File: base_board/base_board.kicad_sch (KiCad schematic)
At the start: 22 parts, among them J1 Conn_ARM_JTAG_SWD_20, U1 STM32F446ZEJx, U2 IS42S16400J-xT, U3 BMI270

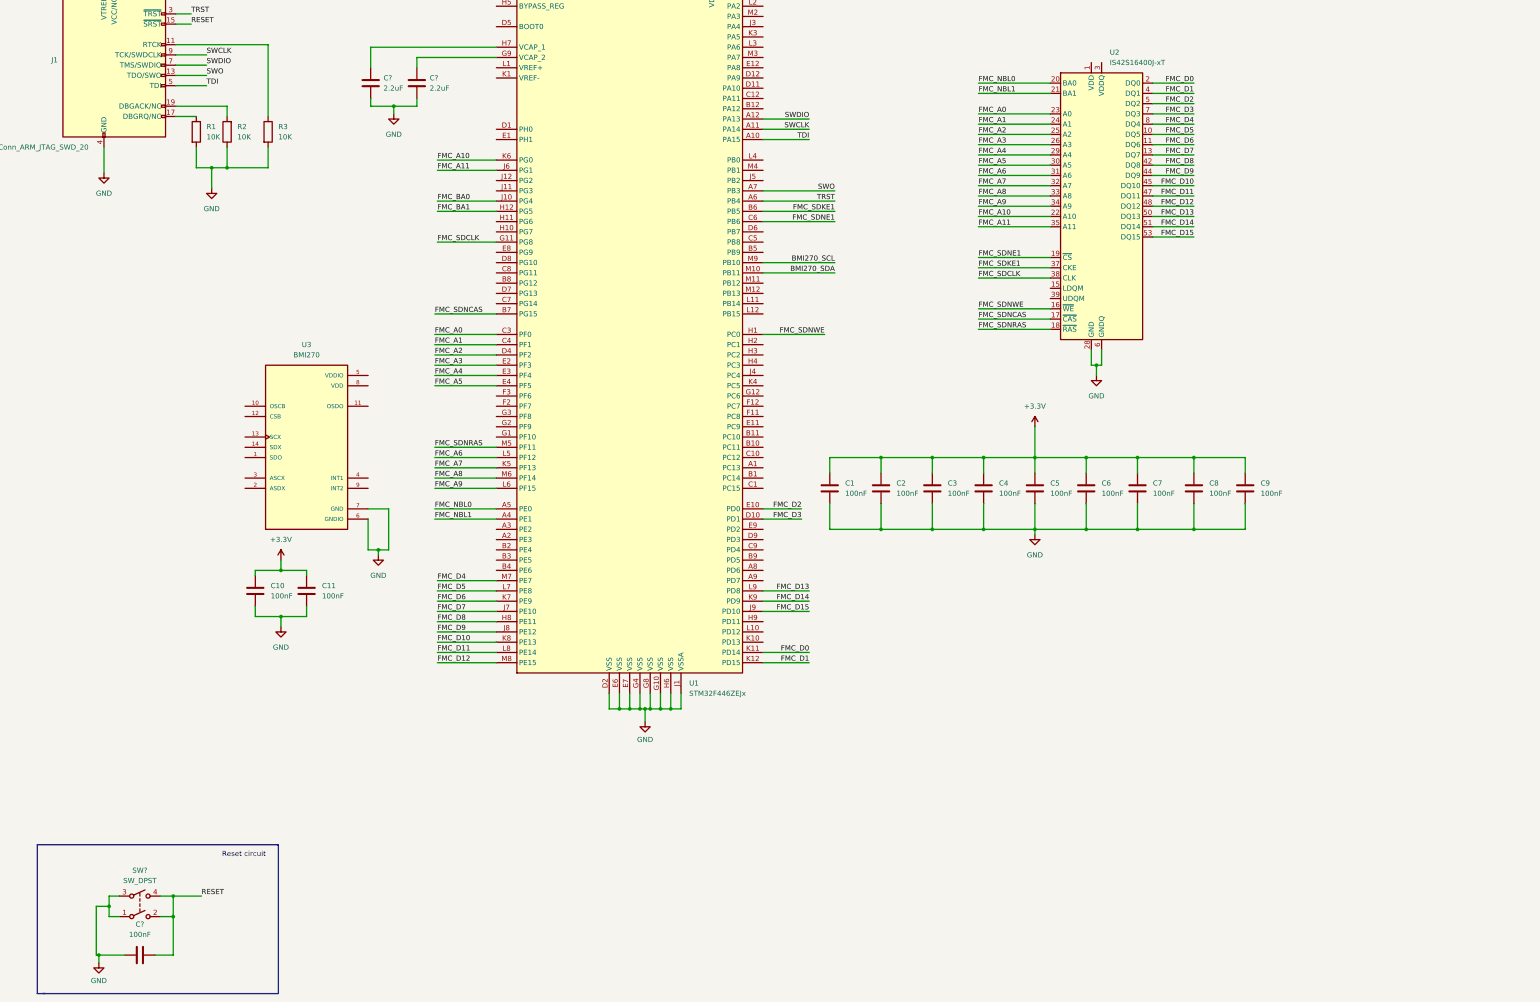
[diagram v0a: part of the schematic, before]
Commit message: [pcb][cube][schematic] added SWD, Crystal, USB
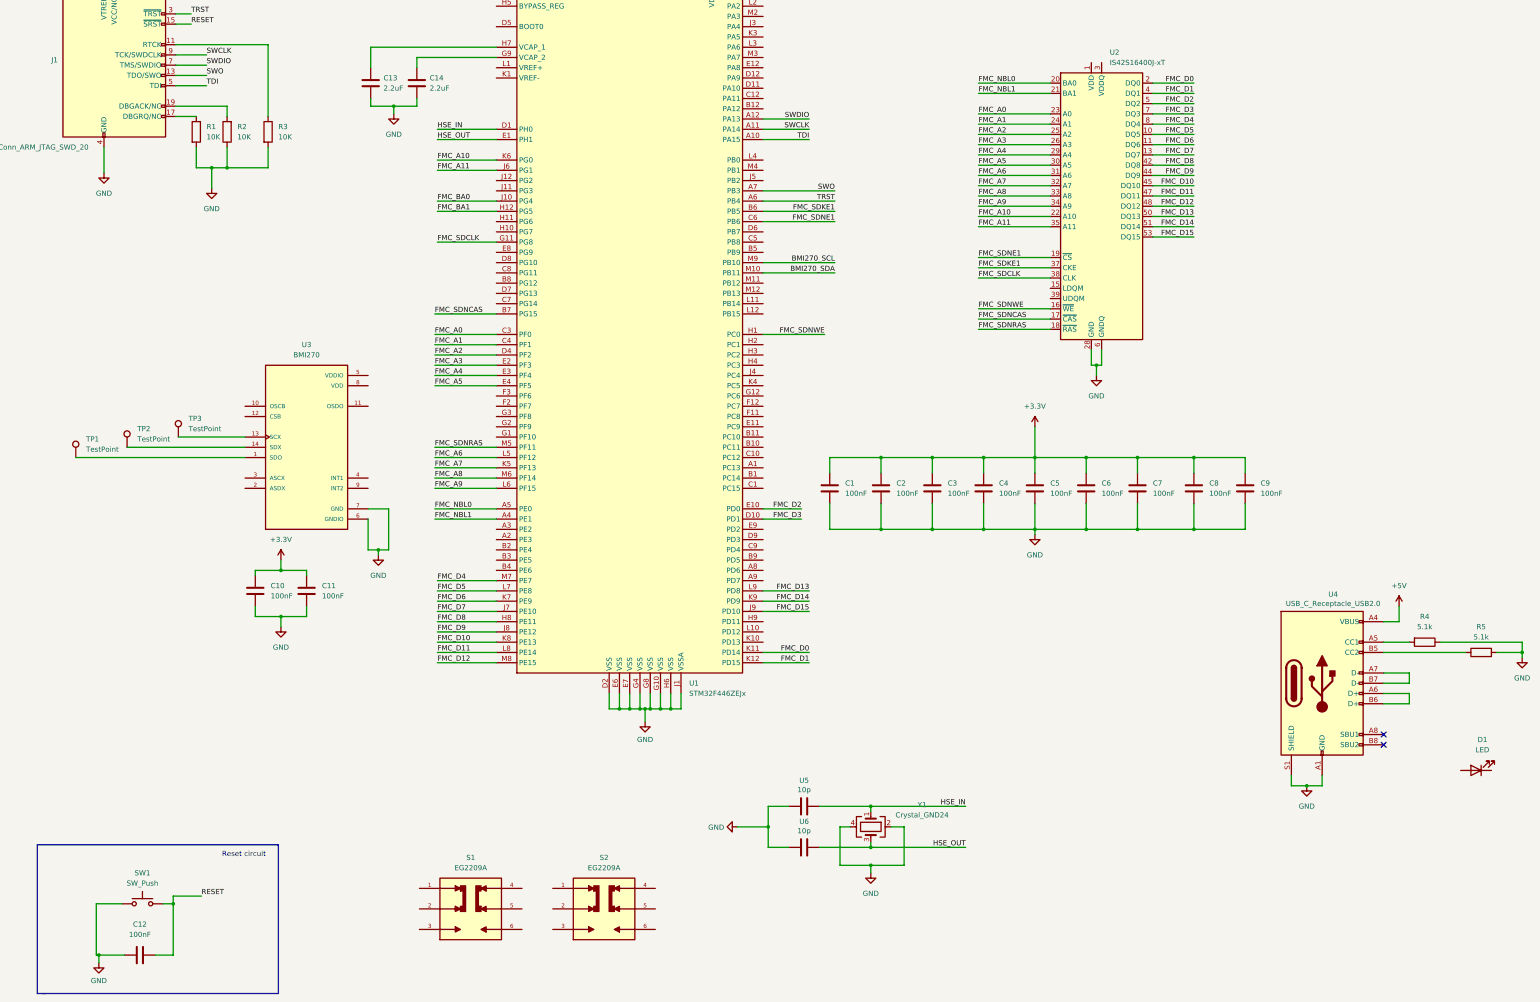
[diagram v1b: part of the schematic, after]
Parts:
- removed SW?: SW_DPST, symbol Switch:SW_DPST
- added D1: LED, LED_SMD:LED_0603_1608Metric, symbol Device:LED
- added R4, R5: 5.1k, Resistor_SMD:R_0603_1608Metric, symbol Device:R
- added S1, S2: EG2209A, project_switch:SW_EG2209A, symbol project_bootswitch:EG2209A
- added SW1: SW_Push, Button_Switch_SMD:SW_Push_1P1T_NO_6x6mm_H9.5mm, symbol Switch:SW_Push
- added TP1, TP2, TP3: TestPoint, TestPoint:TestPoint_Pad_D3.0mm, symbol Connector:TestPoint
- added U4: USB_C_Receptacle_USB2.0, project_typec:USB_C_Receptacle_XKB_U262-16XN-4BVC11, symbol Connector:USB_C_Receptacle_USB2.0
- added U5, U6: 10p, Capacitor_SMD:C_0603_1608Metric, symbol Device:C
- added Y1: Crystal_GND24, Crystal:Crystal_SMD_3225-4Pin_3.2x2.5mm, symbol Device:Crystal_GND24
- gave numbers to parts that had none: 3
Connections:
- net GND: now also R4.1, R5.2, SW1.1, U4.A1 (GND), U4.A12 (GND), U4.B1 (GND), U4.B12 (GND), U4.S1 (SHIELD), U5.2, U6.2, Y1.2, Y1.4
- net RESET: now also SW1.2
- net at U3.1 (SDO): now also TP1.1
- net at U3.13 (SCX): now also TP3.1
- net at U3.14 (SDX): now also TP2.1
- net HSE_IN: now reaches U1.D1 (PH0)
- net HSE_IN: now also U5.1, Y1.1
- net HSE_OUT: now reaches U1.E1 (PH1)
- net HSE_OUT: now also U6.1, Y1.3
- new net: R4.2, U4.A5 (CC1)
- new net: U4.A6 (D+), U4.B6 (D+)
- new net: U4.A7 (D-), U4.B7 (D-)
- new net: R5.1, U4.B5 (CC2)
- new net +5V: U4.A4 (VBUS), U4.A9 (VBUS), U4.B4 (VBUS), U4.B9 (VBUS)
- no-connect marks 0 -> 2

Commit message: [schematic][pcb] added usb, signal leds, LDO
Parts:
- removed S1, S2: EG2209A, project_switch:SW_EG2209A, symbol project_bootswitch:EG2209A
- added C15, C18: 1uF, Capacitor_SMD:C_0603_1608Metric, symbol Device:C
- added C16: 100nF, Capacitor_SMD:C_0603_1608Metric, symbol Device:C
- added C17: 10nF, Capacitor_SMD:C_0603_1608Metric, symbol Device:C
- added D2, D3: LED, LED_SMD:LED_0603_1608Metric, symbol Device:LED
- added JP1, JP2, JP3: SolderJumper_3_Open, Jumper:SolderJumper-3_P1.3mm_Open_RoundedPad1.0x1.5mm, symbol Jumper:SolderJumper_3_Open
- added R10, R6, R7: 10K, Resistor_SMD:R_0603_1608Metric, symbol Device:R
- added R11, R12, R13: 510, Resistor_SMD:R_0603_1608Metric, symbol Device:R
- added R8, R9: 4.7K, Resistor_SMD:R_0603_1608Metric, symbol Device:R
- added TP4: TestPoint, TestPoint:TestPoint_Pad_D3.0mm, symbol Connector:TestPoint
- added U7: LD3985M33R_SOT23, Package_TO_SOT_SMD:SOT-23-5, symbol Regulator_Linear:LD3985M33R_SOT23
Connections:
- net +5V: now also C15.1, C16.2, R11.1, TP4.1, U7.1 (VIN), U7.3 (INH)
- net BMI270_SCL: now also TP2.1, U3.13 (SCX), R9.2
- net BMI270_SDA: now also TP1.1, U3.14 (SDX), R8.2
- net GND: now also D1.1 (K), C15.2, C16.1, C17.2, C18.2, D2.1 (K), D3.1 (K), JP1.1 (A), JP2.1 (A), JP3.1 (A), U7.2 (GND)
- net RESET: now also R10.1
- net +3V3: now reaches TP3.1
- net +3V3: now also U3.12 (CSB), U3.5 (VDDIO), U3.8 (VDD), C18.1, JP1.3 (B), JP2.3 (B), JP3.3 (B), R10.2, R12.1, R8.1, R9.1, U7.5 (VOUT); no longer U3.13 (SCX)
- net at U3.1 (SDO): now also JP3.2 (C); no longer TP1.1
- net BMI270_INT1: now reaches U3.4 (INT1)
- net BMI270_INT1: now also U1.M11 (PB12)
- net BMI270_INT2: now reaches U3.9 (INT2)
- net BMI270_INT2: now also U1.M12 (PB13)
- net USB_D+: now reaches U4.A6 (D+), U4.B6 (D+)
- net USB_D+: now also U1.B12 (PA12)
- net USB_D-: now reaches U4.A7 (D-), U4.B7 (D-)
- net USB_D-: now also U1.C12 (PA11)
- net at D1.2 (A): now also R11.2
- net USART1_RX: now reaches U1.D11 (PA10)
- net USART1_TX: now reaches U1.D12 (PA9)
- net BOOT0: now reaches U1.D5 (BOOT0)
- net BOOT0: now also R6.2
- net BOOT1: now reaches U1.J5 (PB2)
- net BOOT1: now also R7.2
- net HEARTBEAT_LED: now reaches U1.L12 (PB15)
- net HEARTBEAT_LED: now also R13.1
- new net: D2.2 (A), R12.2
- new net: JP2.2 (C), R7.1
- new net: C17.1, U7.4 (BYP)
- new net: JP1.2 (C), R6.1
- new net: D3.2 (A), R13.2
- no-connect marks 2 -> 6
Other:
- note added: "Bootswitch"
- note added: "Crystal"
- note added: "JTAG"
- note added: "Power supply"
- note added: "imu sensor"
- note added: "signal leds"
- moved on the sheet: C10, C11, D1, TP1, TP2, U3, U5, U6, Y1

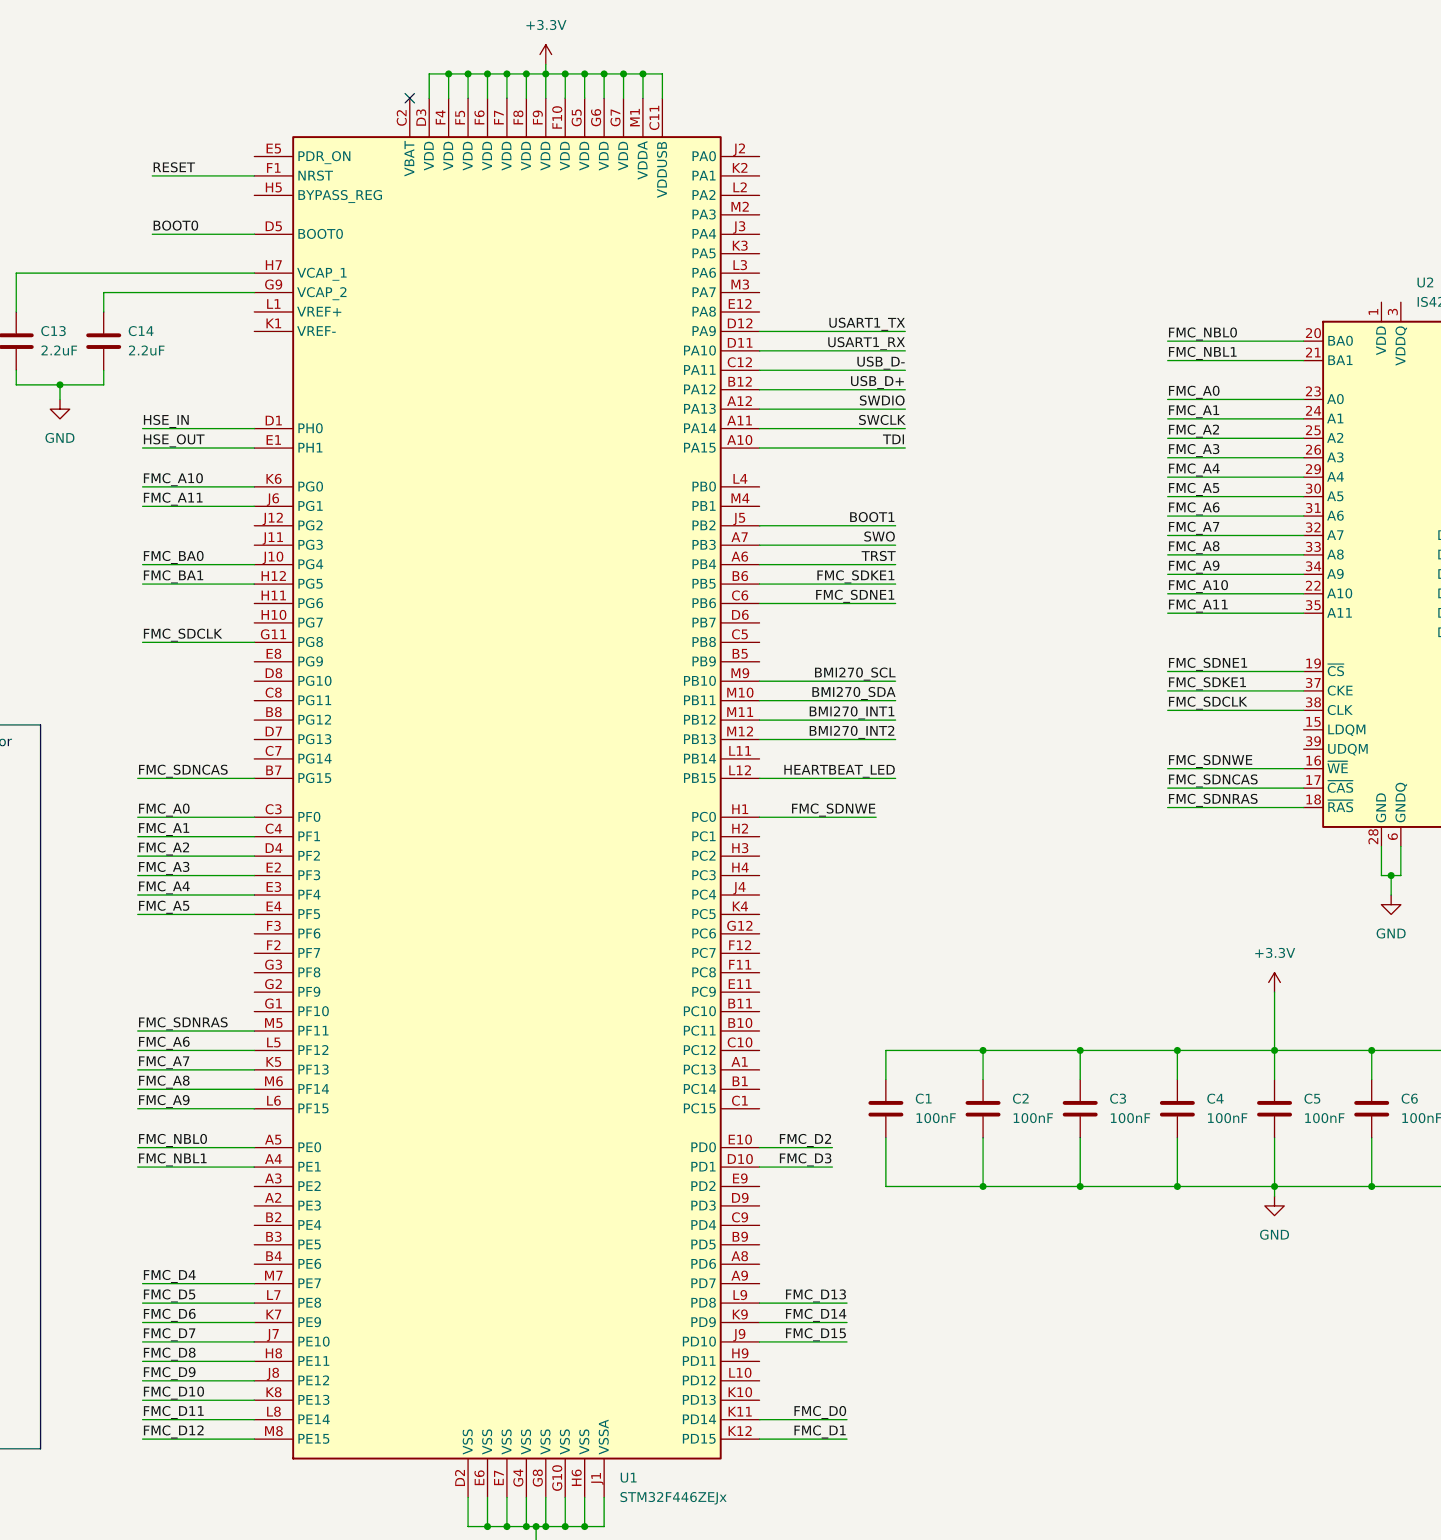
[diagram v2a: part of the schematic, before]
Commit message: [pcb][schematic] fixed sdram connection. added 6 layers stack
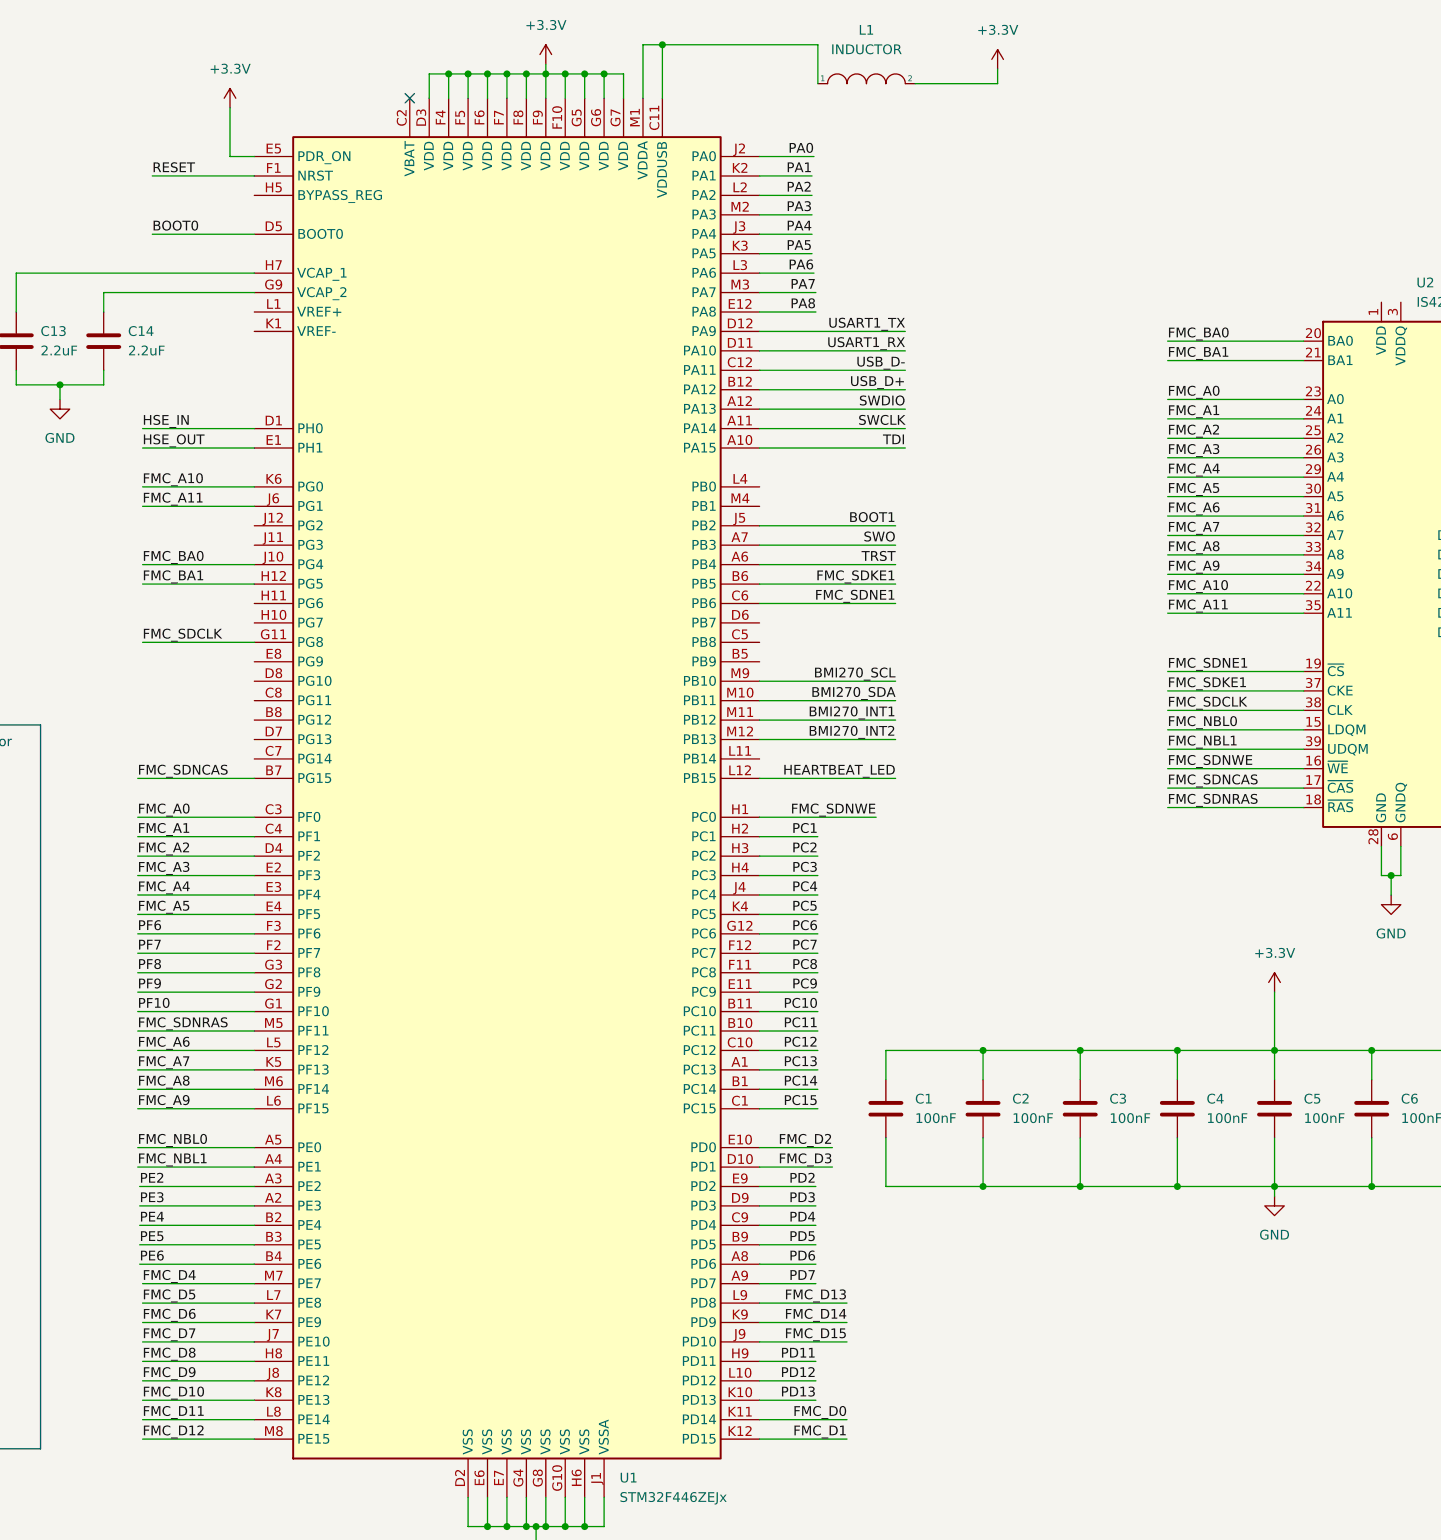
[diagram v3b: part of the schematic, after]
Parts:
- added L1: INDUCTOR, Inductor_SMD:L_0603_1608Metric, symbol pspice:INDUCTOR
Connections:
- net +3.3V: now also U1.E5 (PDR_ON), L1.2; no longer U1.C11 (VDDUSB), U1.M1 (VDDA)
- net FMC_BA0: now also U2.20 (BA0)
- net FMC_BA1: now also U2.21 (BA1)
- net FMC_NBL0: now also U2.15 (LDQM); no longer U2.20 (BA0)
- net FMC_NBL1: now also U2.39 (UDQM); no longer U2.21 (BA1)
- net PC13: now reaches U1.A1 (PC13)
- net PE3: now reaches U1.A2 (PE3)
- net PE2: now reaches U1.A3 (PE2)
- net PD6: now reaches U1.A8 (PD6)
- net PD7: now reaches U1.A9 (PD7)
- net PC14: now reaches U1.B1 (PC14)
- net PC11: now reaches U1.B10 (PC11)
- net PC10: now reaches U1.B11 (PC10)
- net PE4: now reaches U1.B2 (PE4)
- net PE5: now reaches U1.B3 (PE5)
- net PE6: now reaches U1.B4 (PE6)
- net PD5: now reaches U1.B9 (PD5)
- net PC15: now reaches U1.C1 (PC15)
- net PC12: now reaches U1.C10 (PC12)
- net PD4: now reaches U1.C9 (PD4)
- net PD3: now reaches U1.D9 (PD3)
- net PC9: now reaches U1.E11 (PC9)
- net PA8: now reaches U1.E12 (PA8)
- net PD2: now reaches U1.E9 (PD2)
- net PC8: now reaches U1.F11 (PC8)
- net PC7: now reaches U1.F12 (PC7)
- net PF7: now reaches U1.F2 (PF7)
- net PF6: now reaches U1.F3 (PF6)
- net PF10: now reaches U1.G1 (PF10)
- net PC6: now reaches U1.G12 (PC6)
- net PF9: now reaches U1.G2 (PF9)
- net PF8: now reaches U1.G3 (PF8)
- net PC1: now reaches U1.H2 (PC1)
- net PC2: now reaches U1.H3 (PC2)
- net PC3: now reaches U1.H4 (PC3)
- net PD11: now reaches U1.H9 (PD11)
- net PA0: now reaches U1.J2 (PA0)
- net PA4: now reaches U1.J3 (PA4)
- net PC4: now reaches U1.J4 (PC4)
- net PD13: now reaches U1.K10 (PD13)
- net PA1: now reaches U1.K2 (PA1)
- net PA5: now reaches U1.K3 (PA5)
- net PC5: now reaches U1.K4 (PC5)
- net PD12: now reaches U1.L10 (PD12)
- net PA2: now reaches U1.L2 (PA2)
- net PA6: now reaches U1.L3 (PA6)
- net PA3: now reaches U1.M2 (PA3)
- net PA7: now reaches U1.M3 (PA7)
- new net: L1.1, U1.C11 (VDDUSB), U1.M1 (VDDA)

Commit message: [pcb][schematic] added gpio headers&sockets
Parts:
- added J2: Conn_01x20_Pin, Connector_PinHeader_2.54mm:PinHeader_1x20_P2.54mm_Vertical, symbol Connector:Conn_01x20_Pin
- added J3: Conn_01x20_Socket, Connector_PinSocket_2.54mm:PinSocket_1x20_P2.54mm_Vertical, symbol Connector:Conn_01x20_Socket
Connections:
- net PC1: now also J2.1 (Pin_1), J3.1 (Pin_1)
- net PC10: now also J2.10 (Pin_10), J3.10 (Pin_10)
- net PC11: now also J2.11 (Pin_11), J3.11 (Pin_11)
- net PC12: now also J2.12 (Pin_12), J3.12 (Pin_12)
- net PC13: now also J2.13 (Pin_13), J3.13 (Pin_13)
- net PC14: now also J2.14 (Pin_14), J3.14 (Pin_14)
- net PC15: now also J2.15 (Pin_15), J3.15 (Pin_15)
- net PC2: now also J2.2 (Pin_2), J3.2 (Pin_2)
- net PC3: now also J2.3 (Pin_3), J3.3 (Pin_3)
- net PC4: now also J2.4 (Pin_4), J3.4 (Pin_4)
- net PC5: now also J2.5 (Pin_5), J3.5 (Pin_5)
- net PC6: now also J2.6 (Pin_6), J3.6 (Pin_6)
- net PC7: now also J2.7 (Pin_7), J3.7 (Pin_7)
- net PC8: now also J2.8 (Pin_8), J3.8 (Pin_8)
- net PC9: now also J2.9 (Pin_9), J3.9 (Pin_9)
- net PE2: now also J2.20 (Pin_20), J3.20 (Pin_20)
- net PE3: now also J2.19 (Pin_19), J3.19 (Pin_19)
- net PE4: now also J2.18 (Pin_18), J3.18 (Pin_18)
- net PE5: now also J2.17 (Pin_17), J3.17 (Pin_17)
- net PE6: now also J2.16 (Pin_16), J3.16 (Pin_16)
